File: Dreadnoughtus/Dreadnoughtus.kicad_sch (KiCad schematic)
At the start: 403 parts

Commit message: finalized matrix connections
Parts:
- removed D? (x13): DIODE, symbol Simulation_SPICE:DIODE
- removed MX? (x13): MX-NoLED, symbol MX_Alps_Hybrid:MX-NoLED
- added U?: Elite-C, symbol keebio:Elite-C
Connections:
- net row0: now also U?.5 (2/PD1)
- net row1: now also U?.6 (3/PD0)
- net row10: now also U?.18 (A1/PF6)
- net row11: now also U?.17 (A0/PF7)
- net row12: now also U?.16 (15/PB1)
- net row13: now also U?.15 (14/PB3)
- net row2: now also U?.7 (4/PD4)
- net row3: now also U?.8 (5/PC6)
- net row4: now also U?.9 (6/PD7)
- net row5: now also U?.10 (7/PE6)
- net row6: now also U?.11 (8/PB4)
- net row7: now also U?.12 (9/PB5)
- net row8: now also U?.20 (A3/PF4)
- net row9: now also U?.19 (A2/PF5)
- net at D?.2 (K), D?.2 (K), D?.2 (K)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: now also D?.1 (A) (x10)
- net at D?.2 (K), D?.2 (K): now also D?.1 (A)
- net at D?.2 (K), D?.2 (K), D?.2 (K)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: now also D?.1 (A), D?.2 (K), D?.2 (K), D?.2 (K), D?.2 (K), D?.2 (K), D?.2 (K), D?.2 (K)
- new net row14: U?.14 (16/PB2)
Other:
- moved on the sheet: D?, MX?

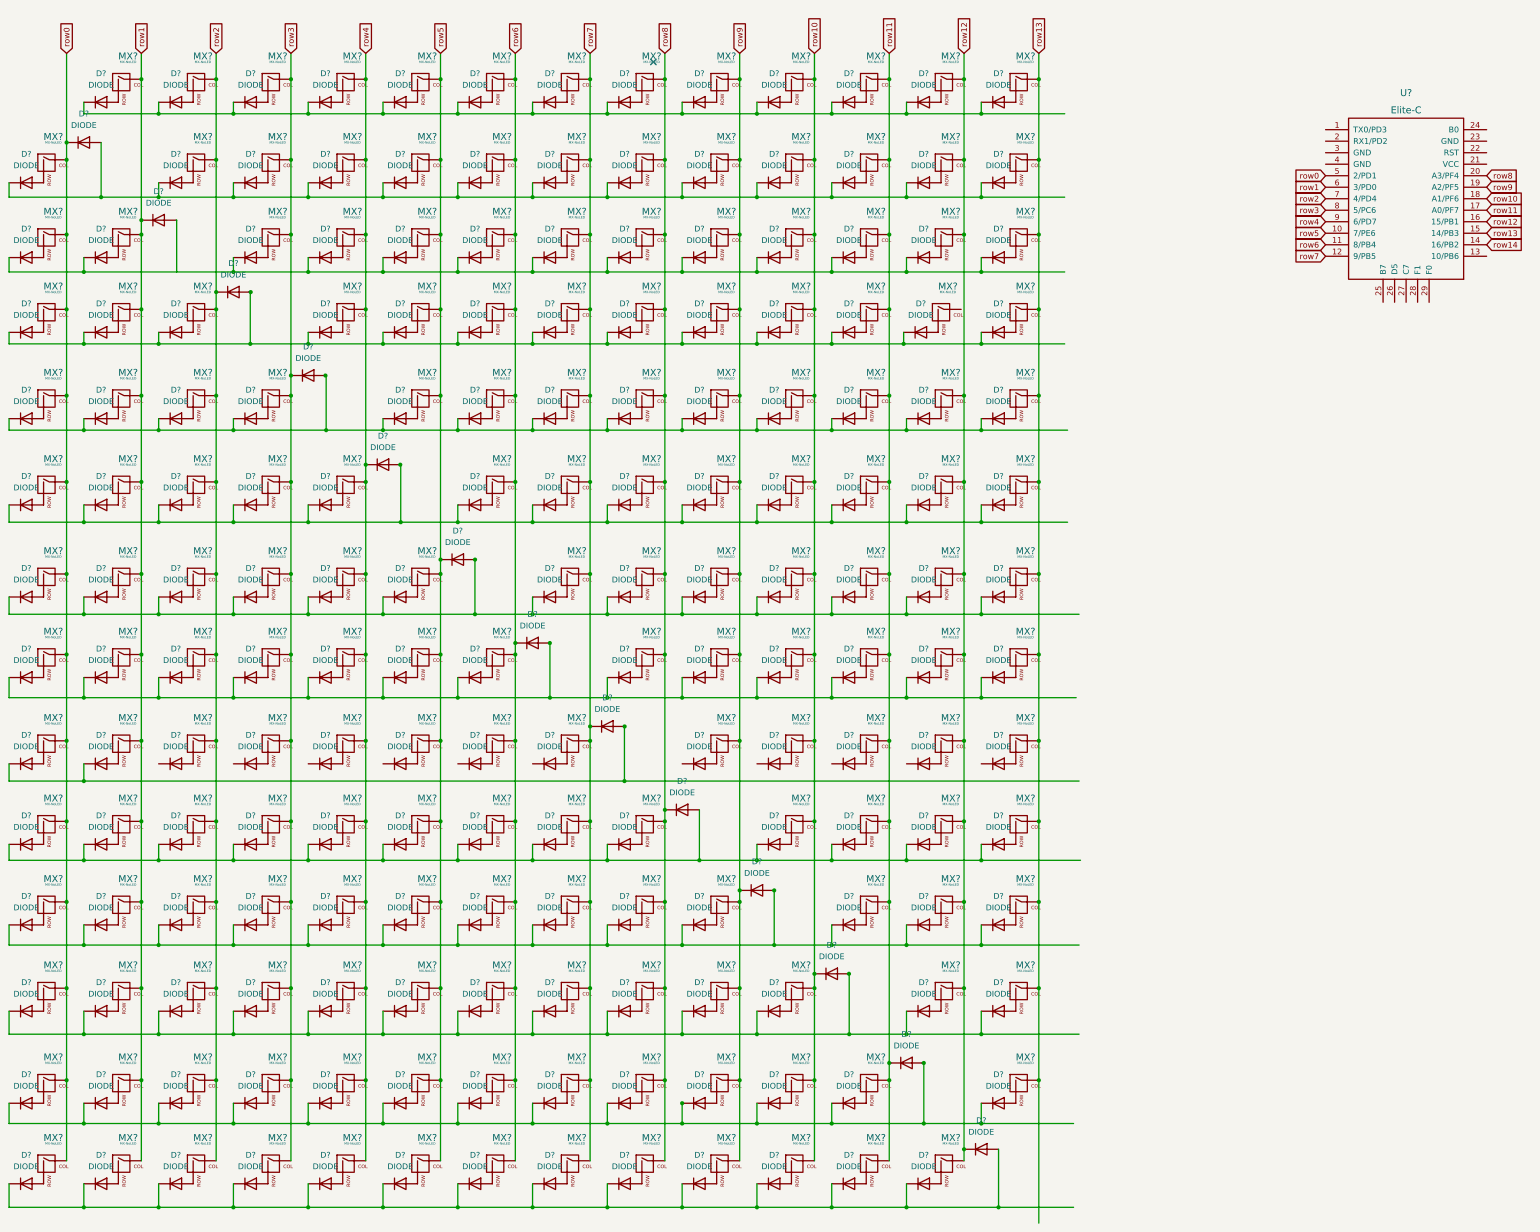
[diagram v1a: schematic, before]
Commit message: named switches and switch diodes, added i2c start schematic
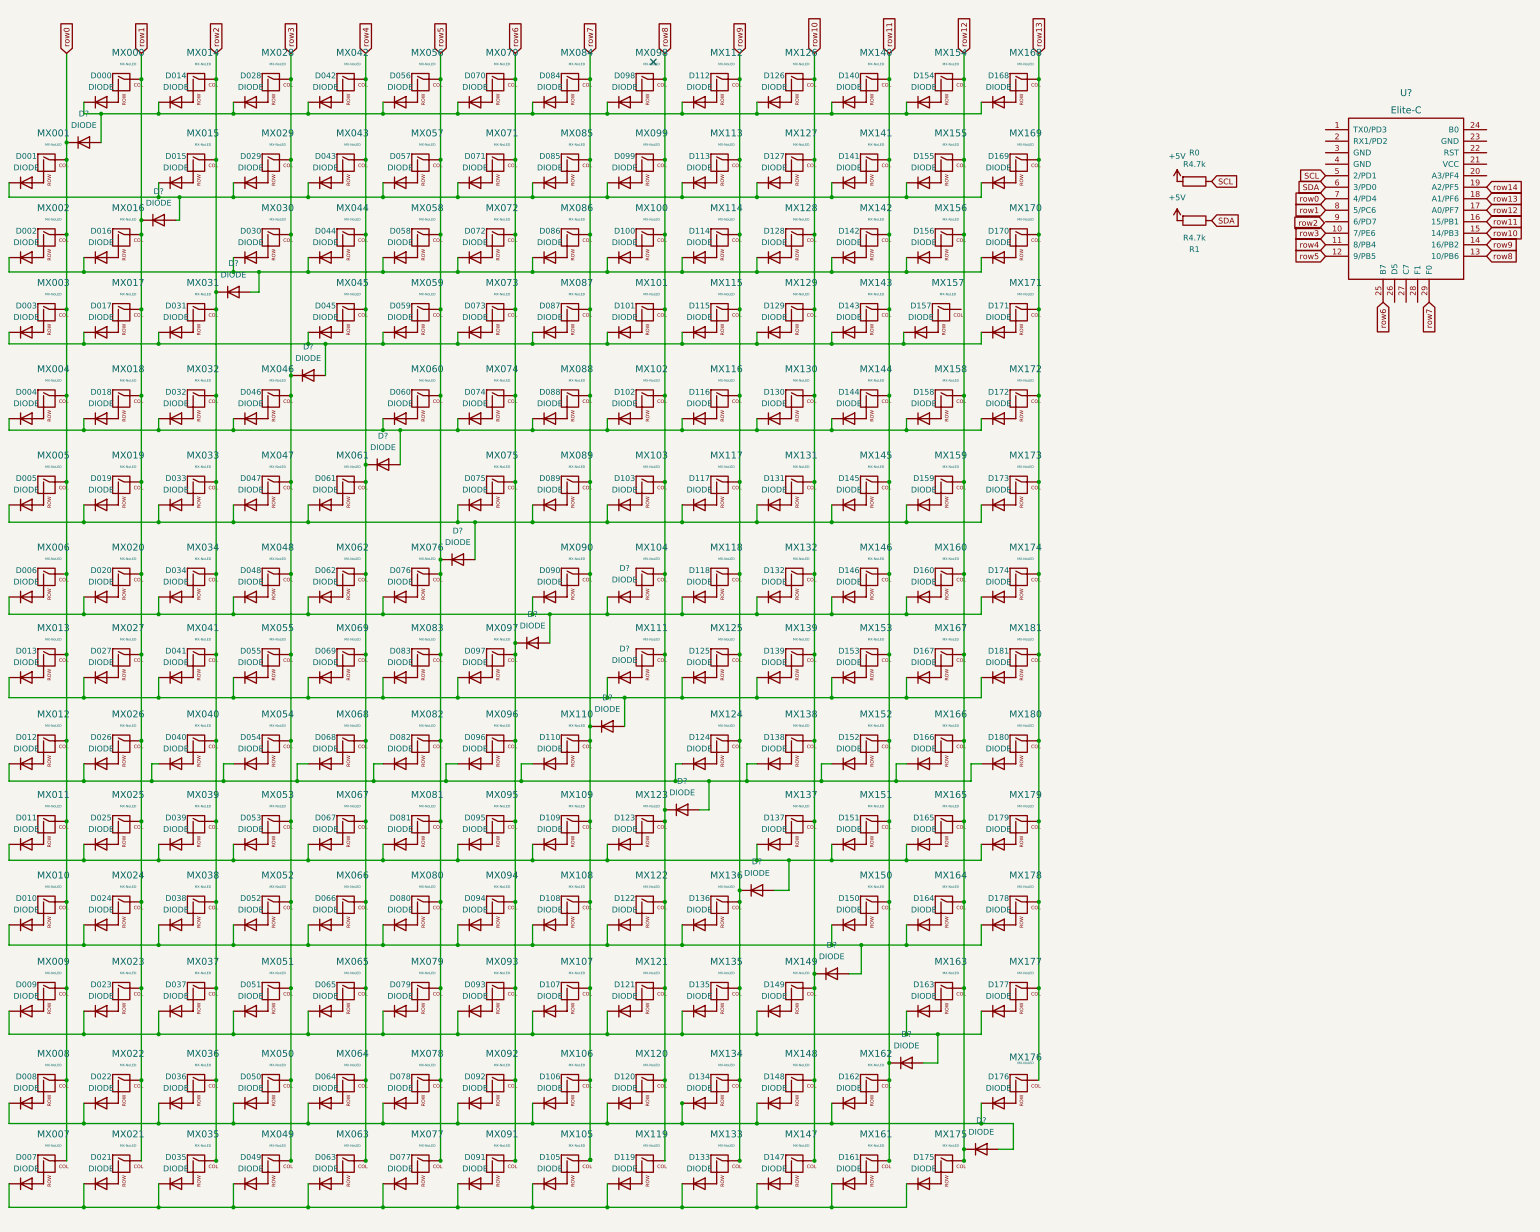
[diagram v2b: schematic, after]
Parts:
- added R0, R1: R4.7k, symbol Device:R
- gave numbers to parts that had none: 362
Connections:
- net row0: now also U?.7 (4/PD4); no longer U?.5 (2/PD1)
- net row1: now also U?.8 (5/PC6); no longer U?.6 (3/PD0)
- net row10: now also U?.15 (14/PB3); no longer U?.18 (A1/PF6)
- net row11: now also U?.16 (15/PB1); no longer U?.17 (A0/PF7)
- net row12: now also U?.17 (A0/PF7); no longer U?.16 (15/PB1)
- net row13: now also U?.18 (A1/PF6); no longer U?.15 (14/PB3)
- net row14: now also U?.19 (A2/PF5); no longer U?.14 (16/PB2)
- net row2: no longer U?.7 (4/PD4)
- net row3: now also U?.10 (7/PE6); no longer U?.8 (5/PC6)
- net row4: now also U?.11 (8/PB4); no longer U?.9 (6/PD7)
- net row5: now also U?.12 (9/PB5); no longer U?.10 (7/PE6)
- net row6: now also U?.25 (B7); no longer U?.11 (8/PB4)
- net row7: now also U?.29 (F0); no longer U?.12 (9/PB5)
- net row8: now also U?.13 (10/PB6); no longer U?.20 (A3/PF4)
- net row9: now also U?.14 (16/PB2); no longer U?.19 (A2/PF5)
- net at D005.2 (K), D019.2 (K), D033.2 (K)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: now also D?.1 (A); no longer D?.1 (A)
- net at D004.2 (K), D018.2 (K), D032.2 (K)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: now also D?.1 (A); no longer D?.1 (A)
- net at D000.2 (K), D014.2 (K), D028.2 (K)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: now also D?.1 (A)
- net at D011.2 (K), D025.2 (K), D039.2 (K)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: now also D?.1 (A); no longer D?.1 (A)
- net at D002.2 (K), D016.2 (K), D030.2 (K)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: now also D?.1 (A)
- net at D003.2 (K), D017.2 (K), D031.2 (K)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: now also D?.1 (A); no longer D?.1 (A)
- net at D010.2 (K), D024.2 (K), D038.2 (K)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: now also D?.1 (A); no longer D?.1 (A)
- net at D007.2 (K), D021.2 (K), D035.2 (K)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: no longer D?.1 (A)
- net at D006.2 (K), D020.2 (K), D034.2 (K)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: now also D?.1 (A); no longer D?.1 (A)
- net at D008.2 (K), D022.2 (K), D036.2 (K)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: now also D?.1 (A); no longer D?.1 (A)
- net at D009.2 (K), D023.2 (K), D037.2 (K)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: now also D?.1 (A); no longer D?.1 (A)
- net at D001.2 (K), D015.2 (K), D029.2 (K)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: now also D?.1 (A); no longer D?.1 (A)
- net at D040.2 (K): now also D012.2 (K), D026.2 (K), D054.2 (K), D068.2 (K), D082.2 (K), D096.2 (K), D110.2 (K), D124.2 (K), D138.2 (K), D152.2 (K), D166.2 (K), D180.2 (K), D?.1 (A)
- net at D013.2 (K), D027.2 (K), D041.2 (K)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: now also D?.1 (A); no longer D?.1 (A)
- new net +5V: R0.2, R1.2
- new net SCL: R0.1, U?.5 (2/PD1)
- new net SDA: R1.1, U?.6 (3/PD0)

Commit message: arranged switches on pcb
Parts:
- added U2, U3: PRTR5V0U2X, Keebio-Parts:I2C_Breakout, symbol keebio:PRTR5V0U2X
- D0: renamed from D000; footprint (none) -> Keebio-Parts:Diode-dual
- D1: renamed from D001; footprint (none) -> Keebio-Parts:Diode-dual
- D10: renamed from D010; footprint (none) -> Keebio-Parts:Diode-dual
- D100, D101, D102, D103, D105, D106, D107, D108, D109, D110, D112, D113, D114, D115, D116, D117, D118, D119, D120, D121, D122, D123, D124, D125, D126, D127, D128, D129, D130, D131, D132, D133, D134, D135, D136, D137, D138, D139, D140, D141, D142, D143, D144, D145, D146, D147, D148, D149, D150, D151, D152, D153, D154, D155, D156, D157, D158, D159, D160, D161, D162, D163, D164, D165, D166, D167, D168, D169, D170, D171, D172, D173, D174, D175, D176, D177, D178, D179, D180, D181: footprint (none) -> Keebio-Parts:Diode-dual
- D104, D111, D201, D202, D203, D204, D205, D206, D207, D208, D209, D210, D211, D212, D213: renamed from D?; footprint (none) -> Keebio-Parts:Diode-dual
- D11: renamed from D011; footprint (none) -> Keebio-Parts:Diode-dual
- D12: renamed from D012; footprint (none) -> Keebio-Parts:Diode-dual
- D13: renamed from D013; footprint (none) -> Keebio-Parts:Diode-dual
- D14: renamed from D014; footprint (none) -> Keebio-Parts:Diode-dual
- D15: renamed from D015; footprint (none) -> Keebio-Parts:Diode-dual
- D16: renamed from D016; footprint (none) -> Keebio-Parts:Diode-dual
- D17: renamed from D017; footprint (none) -> Keebio-Parts:Diode-dual
- D18: renamed from D018; footprint (none) -> Keebio-Parts:Diode-dual
- D19: renamed from D019; footprint (none) -> Keebio-Parts:Diode-dual
- D2: renamed from D002; footprint (none) -> Keebio-Parts:Diode-dual
- D20: renamed from D020; footprint (none) -> Keebio-Parts:Diode-dual
- D21: renamed from D021; footprint (none) -> Keebio-Parts:Diode-dual
- D22: renamed from D022; footprint (none) -> Keebio-Parts:Diode-dual
- D23: renamed from D023; footprint (none) -> Keebio-Parts:Diode-dual
- D24: renamed from D024; footprint (none) -> Keebio-Parts:Diode-dual
- D25: renamed from D025; footprint (none) -> Keebio-Parts:Diode-dual
- D26: renamed from D026; footprint (none) -> Keebio-Parts:Diode-dual
- D27: renamed from D027; footprint (none) -> Keebio-Parts:Diode-dual
- D28: renamed from D028; footprint (none) -> Keebio-Parts:Diode-dual
- D29: renamed from D029; footprint (none) -> Keebio-Parts:Diode-dual
- D3: renamed from D003; footprint (none) -> Keebio-Parts:Diode-dual
- D30: renamed from D030; footprint (none) -> Keebio-Parts:Diode-dual
- D31: renamed from D031; footprint (none) -> Keebio-Parts:Diode-dual
- D32: renamed from D032; footprint (none) -> Keebio-Parts:Diode-dual
- D33: renamed from D033; footprint (none) -> Keebio-Parts:Diode-dual
- D34: renamed from D034; footprint (none) -> Keebio-Parts:Diode-dual
- D35: renamed from D035; footprint (none) -> Keebio-Parts:Diode-dual
- D36: renamed from D036; footprint (none) -> Keebio-Parts:Diode-dual
- D37: renamed from D037; footprint (none) -> Keebio-Parts:Diode-dual
- D38: renamed from D038; footprint (none) -> Keebio-Parts:Diode-dual
- D39: renamed from D039; footprint (none) -> Keebio-Parts:Diode-dual
- D4: renamed from D004; footprint (none) -> Keebio-Parts:Diode-dual
- D40: renamed from D040; footprint (none) -> Keebio-Parts:Diode-dual
- D41: renamed from D041; footprint (none) -> Keebio-Parts:Diode-dual
- D42: renamed from D042; footprint (none) -> Keebio-Parts:Diode-dual
- D43: renamed from D043; footprint (none) -> Keebio-Parts:Diode-dual
- D44: renamed from D044; footprint (none) -> Keebio-Parts:Diode-dual
- D45: renamed from D045; footprint (none) -> Keebio-Parts:Diode-dual
- D46: renamed from D046; footprint (none) -> Keebio-Parts:Diode-dual
- D47: renamed from D047; footprint (none) -> Keebio-Parts:Diode-dual
- D48: renamed from D048; footprint (none) -> Keebio-Parts:Diode-dual
- D49: renamed from D049; footprint (none) -> Keebio-Parts:Diode-dual
- D5: renamed from D005; footprint (none) -> Keebio-Parts:Diode-dual
- D50: renamed from D050; footprint (none) -> Keebio-Parts:Diode-dual
- D51: renamed from D051; footprint (none) -> Keebio-Parts:Diode-dual
- D52: renamed from D052; footprint (none) -> Keebio-Parts:Diode-dual
- D53: renamed from D053; footprint (none) -> Keebio-Parts:Diode-dual
- D54: renamed from D054; footprint (none) -> Keebio-Parts:Diode-dual
- D55: renamed from D055; footprint (none) -> Keebio-Parts:Diode-dual
- D56: renamed from D056; footprint (none) -> Keebio-Parts:Diode-dual
- D57: renamed from D057; footprint (none) -> Keebio-Parts:Diode-dual
- D58: renamed from D058; footprint (none) -> Keebio-Parts:Diode-dual
- D59: renamed from D059; footprint (none) -> Keebio-Parts:Diode-dual
- D6: renamed from D006; footprint (none) -> Keebio-Parts:Diode-dual
- D60: renamed from D060; footprint (none) -> Keebio-Parts:Diode-dual
- D61: renamed from D061; footprint (none) -> Keebio-Parts:Diode-dual
- D62: renamed from D062; footprint (none) -> Keebio-Parts:Diode-dual
- D63: renamed from D063; footprint (none) -> Keebio-Parts:Diode-dual
- D64: renamed from D064; footprint (none) -> Keebio-Parts:Diode-dual
- D65: renamed from D065; footprint (none) -> Keebio-Parts:Diode-dual
- D66: renamed from D066; footprint (none) -> Keebio-Parts:Diode-dual
- D67: renamed from D067; footprint (none) -> Keebio-Parts:Diode-dual
- D68: renamed from D068; footprint (none) -> Keebio-Parts:Diode-dual
- D69: renamed from D069; footprint (none) -> Keebio-Parts:Diode-dual
- D7: renamed from D007; footprint (none) -> Keebio-Parts:Diode-dual
- D70: renamed from D070; footprint (none) -> Keebio-Parts:Diode-dual
- D71: renamed from D071; footprint (none) -> Keebio-Parts:Diode-dual
- D72: renamed from D072; footprint (none) -> Keebio-Parts:Diode-dual
- D73: renamed from D073; footprint (none) -> Keebio-Parts:Diode-dual
- D74: renamed from D074; footprint (none) -> Keebio-Parts:Diode-dual
- D75: renamed from D075; footprint (none) -> Keebio-Parts:Diode-dual
- D76: renamed from D076; footprint (none) -> Keebio-Parts:Diode-dual
- D77: renamed from D077; footprint (none) -> Keebio-Parts:Diode-dual
- D78: renamed from D078; footprint (none) -> Keebio-Parts:Diode-dual
- D79: renamed from D079; footprint (none) -> Keebio-Parts:Diode-dual
- D8: renamed from D008; footprint (none) -> Keebio-Parts:Diode-dual
- D80: renamed from D080; footprint (none) -> Keebio-Parts:Diode-dual
- D81: renamed from D081; footprint (none) -> Keebio-Parts:Diode-dual
- D82: renamed from D082; footprint (none) -> Keebio-Parts:Diode-dual
- D83: renamed from D083; footprint (none) -> Keebio-Parts:Diode-dual
- D84: renamed from D084; footprint (none) -> Keebio-Parts:Diode-dual
- D85: renamed from D085; footprint (none) -> Keebio-Parts:Diode-dual
- D86: renamed from D086; footprint (none) -> Keebio-Parts:Diode-dual
- D87: renamed from D087; footprint (none) -> Keebio-Parts:Diode-dual
- D88: renamed from D088; footprint (none) -> Keebio-Parts:Diode-dual
- D89: renamed from D089; footprint (none) -> Keebio-Parts:Diode-dual
- D9: renamed from D009; footprint (none) -> Keebio-Parts:Diode-dual
- D90: renamed from D090; footprint (none) -> Keebio-Parts:Diode-dual
- D91: renamed from D091; footprint (none) -> Keebio-Parts:Diode-dual
- D92: renamed from D092; footprint (none) -> Keebio-Parts:Diode-dual
- D93: renamed from D093; footprint (none) -> Keebio-Parts:Diode-dual
- D94: renamed from D094; footprint (none) -> Keebio-Parts:Diode-dual
- D95: renamed from D095; footprint (none) -> Keebio-Parts:Diode-dual
- D96: renamed from D096; footprint (none) -> Keebio-Parts:Diode-dual
- D97: renamed from D097; footprint (none) -> Keebio-Parts:Diode-dual
- D98: renamed from D098; footprint (none) -> Keebio-Parts:Diode-dual
- D99: renamed from D099; footprint (none) -> Keebio-Parts:Diode-dual
- MX0: renamed from MX000; footprint (none) -> MX_Alps_Hybrid:MXOnly-1U-Hotswap
- MX1: renamed from MX001; footprint (none) -> MX_Alps_Hybrid:MXOnly-1U-Hotswap
- MX10: renamed from MX010; footprint (none) -> MX_Alps_Hybrid:MXOnly-1U-Hotswap
- MX100, MX101, MX102, MX103, MX104, MX105, MX106, MX107, MX108, MX109, MX110, MX111, MX112, MX113, MX114, MX115, MX116, MX117, MX118, MX119, MX120, MX121, MX122, MX123, MX124, MX125, MX126, MX127, MX128, MX129, MX130, MX131, MX132, MX133, MX134, MX135, MX136, MX137, MX138, MX139, MX140, MX141, MX142, MX143, MX144, MX145, MX146, MX147, MX148, MX149, MX150, MX151, MX152, MX153, MX154, MX155, MX156, MX157, MX158, MX159, MX160, MX161, MX162, MX163, MX164, MX165, MX166, MX167, MX168, MX169, MX170, MX171, MX172, MX173, MX174, MX175, MX176, MX177, MX178, MX179, MX180, MX181: footprint (none) -> MX_Alps_Hybrid:MXOnly-1U-Hotswap
- MX11: renamed from MX011; footprint (none) -> MX_Alps_Hybrid:MXOnly-1U-Hotswap
- MX12: renamed from MX012; footprint (none) -> MX_Alps_Hybrid:MXOnly-1U-Hotswap
- MX13: renamed from MX013; footprint (none) -> MX_Alps_Hybrid:MXOnly-1U-Hotswap
- MX14: renamed from MX014; footprint (none) -> MX_Alps_Hybrid:MXOnly-1U-Hotswap
- MX15: renamed from MX015; footprint (none) -> MX_Alps_Hybrid:MXOnly-1U-Hotswap
- MX16: renamed from MX016; footprint (none) -> MX_Alps_Hybrid:MXOnly-1U-Hotswap
- MX17: renamed from MX017; footprint (none) -> MX_Alps_Hybrid:MXOnly-1U-Hotswap
- MX18: renamed from MX018; footprint (none) -> MX_Alps_Hybrid:MXOnly-1U-Hotswap
- MX19: renamed from MX019; footprint (none) -> MX_Alps_Hybrid:MXOnly-1U-Hotswap
- MX2: renamed from MX002; footprint (none) -> MX_Alps_Hybrid:MXOnly-1U-Hotswap
- MX20: renamed from MX020; footprint (none) -> MX_Alps_Hybrid:MXOnly-1U-Hotswap
- MX21: renamed from MX021; footprint (none) -> MX_Alps_Hybrid:MXOnly-1U-Hotswap
- MX22: renamed from MX022; footprint (none) -> MX_Alps_Hybrid:MXOnly-1U-Hotswap
- MX23: renamed from MX023; footprint (none) -> MX_Alps_Hybrid:MXOnly-1U-Hotswap
- MX24: renamed from MX024; footprint (none) -> MX_Alps_Hybrid:MXOnly-1U-Hotswap
- MX25: renamed from MX025; footprint (none) -> MX_Alps_Hybrid:MXOnly-1U-Hotswap
- MX26: renamed from MX026; footprint (none) -> MX_Alps_Hybrid:MXOnly-1U-Hotswap
- MX27: renamed from MX027; footprint (none) -> MX_Alps_Hybrid:MXOnly-1U-Hotswap
- MX28: renamed from MX028; footprint (none) -> MX_Alps_Hybrid:MXOnly-1U-Hotswap
- MX29: renamed from MX029; footprint (none) -> MX_Alps_Hybrid:MXOnly-1U-Hotswap
- MX3: renamed from MX003; footprint (none) -> MX_Alps_Hybrid:MXOnly-1U-Hotswap
- MX30: renamed from MX030; footprint (none) -> MX_Alps_Hybrid:MXOnly-1U-Hotswap
- MX31: renamed from MX031; footprint (none) -> MX_Alps_Hybrid:MXOnly-1U-Hotswap
- MX32: renamed from MX032; footprint (none) -> MX_Alps_Hybrid:MXOnly-1U-Hotswap
- MX33: renamed from MX033; footprint (none) -> MX_Alps_Hybrid:MXOnly-1U-Hotswap
- MX34: renamed from MX034; footprint (none) -> MX_Alps_Hybrid:MXOnly-1U-Hotswap
- MX35: renamed from MX035; footprint (none) -> MX_Alps_Hybrid:MXOnly-1U-Hotswap
- MX36: renamed from MX036; footprint (none) -> MX_Alps_Hybrid:MXOnly-1U-Hotswap
- MX37: renamed from MX037; footprint (none) -> MX_Alps_Hybrid:MXOnly-1U-Hotswap
- MX38: renamed from MX038; footprint (none) -> MX_Alps_Hybrid:MXOnly-1U-Hotswap
- MX39: renamed from MX039; footprint (none) -> MX_Alps_Hybrid:MXOnly-1U-Hotswap
- MX4: renamed from MX004; footprint (none) -> MX_Alps_Hybrid:MXOnly-1U-Hotswap
- MX40: renamed from MX040; footprint (none) -> MX_Alps_Hybrid:MXOnly-1U-Hotswap
- MX41: renamed from MX041; footprint (none) -> MX_Alps_Hybrid:MXOnly-1U-Hotswap
- MX42: renamed from MX042; footprint (none) -> MX_Alps_Hybrid:MXOnly-1U-Hotswap
- MX43: renamed from MX043; footprint (none) -> MX_Alps_Hybrid:MXOnly-1U-Hotswap
- MX44: renamed from MX044; footprint (none) -> MX_Alps_Hybrid:MXOnly-1U-Hotswap
- MX45: renamed from MX045; footprint (none) -> MX_Alps_Hybrid:MXOnly-1U-Hotswap
- MX46: renamed from MX046; footprint (none) -> MX_Alps_Hybrid:MXOnly-1U-Hotswap
- MX47: renamed from MX047; footprint (none) -> MX_Alps_Hybrid:MXOnly-1U-Hotswap
- MX48: renamed from MX048; footprint (none) -> MX_Alps_Hybrid:MXOnly-1U-Hotswap
- MX49: renamed from MX049; footprint (none) -> MX_Alps_Hybrid:MXOnly-1U-Hotswap
- MX5: renamed from MX005; footprint (none) -> MX_Alps_Hybrid:MXOnly-1U-Hotswap
- MX50: renamed from MX050; footprint (none) -> MX_Alps_Hybrid:MXOnly-1U-Hotswap
- MX51: renamed from MX051; footprint (none) -> MX_Alps_Hybrid:MXOnly-1U-Hotswap
- MX52: renamed from MX052; footprint (none) -> MX_Alps_Hybrid:MXOnly-1U-Hotswap
- MX53: renamed from MX053; footprint (none) -> MX_Alps_Hybrid:MXOnly-1U-Hotswap
- MX54: renamed from MX054; footprint (none) -> MX_Alps_Hybrid:MXOnly-1U-Hotswap
- MX55: renamed from MX055; footprint (none) -> MX_Alps_Hybrid:MXOnly-1U-Hotswap
- MX56: renamed from MX056; footprint (none) -> MX_Alps_Hybrid:MXOnly-1U-Hotswap
- MX57: renamed from MX057; footprint (none) -> MX_Alps_Hybrid:MXOnly-1U-Hotswap
- MX58: renamed from MX058; footprint (none) -> MX_Alps_Hybrid:MXOnly-1U-Hotswap
- MX59: renamed from MX059; footprint (none) -> MX_Alps_Hybrid:MXOnly-1U-Hotswap
- MX6: renamed from MX006; footprint (none) -> MX_Alps_Hybrid:MXOnly-1U-Hotswap
- MX60: renamed from MX060; footprint (none) -> MX_Alps_Hybrid:MXOnly-1U-Hotswap
- MX61: renamed from MX061; footprint (none) -> MX_Alps_Hybrid:MXOnly-1U-Hotswap
- MX62: renamed from MX062; footprint (none) -> MX_Alps_Hybrid:MXOnly-1U-Hotswap
- MX63: renamed from MX063; footprint (none) -> MX_Alps_Hybrid:MXOnly-1U-Hotswap
- MX64: renamed from MX064; footprint (none) -> MX_Alps_Hybrid:MXOnly-1U-Hotswap
- MX65: renamed from MX065; footprint (none) -> MX_Alps_Hybrid:MXOnly-1U-Hotswap
- MX66: renamed from MX066; footprint (none) -> MX_Alps_Hybrid:MXOnly-1U-Hotswap
- MX67: renamed from MX067; footprint (none) -> MX_Alps_Hybrid:MXOnly-1U-Hotswap
- MX68: renamed from MX068; footprint (none) -> MX_Alps_Hybrid:MXOnly-1U-Hotswap
- MX69: renamed from MX069; footprint (none) -> MX_Alps_Hybrid:MXOnly-1U-Hotswap
- MX7: renamed from MX007; footprint (none) -> MX_Alps_Hybrid:MXOnly-1U-Hotswap
- MX70: renamed from MX070; footprint (none) -> MX_Alps_Hybrid:MXOnly-1U-Hotswap
- MX71: renamed from MX071; footprint (none) -> MX_Alps_Hybrid:MXOnly-1U-Hotswap
- MX72: renamed from MX072; footprint (none) -> MX_Alps_Hybrid:MXOnly-1U-Hotswap
- MX73: renamed from MX073; footprint (none) -> MX_Alps_Hybrid:MXOnly-1U-Hotswap
- MX74: renamed from MX074; footprint (none) -> MX_Alps_Hybrid:MXOnly-1U-Hotswap
- MX75: renamed from MX075; footprint (none) -> MX_Alps_Hybrid:MXOnly-1U-Hotswap
- MX76: renamed from MX076; footprint (none) -> MX_Alps_Hybrid:MXOnly-1U-Hotswap
- MX77: renamed from MX077; footprint (none) -> MX_Alps_Hybrid:MXOnly-1U-Hotswap
- MX78: renamed from MX078; footprint (none) -> MX_Alps_Hybrid:MXOnly-1U-Hotswap
- MX79: renamed from MX079; footprint (none) -> MX_Alps_Hybrid:MXOnly-1U-Hotswap
- MX8: renamed from MX008; footprint (none) -> MX_Alps_Hybrid:MXOnly-1U-Hotswap
- MX80: renamed from MX080; footprint (none) -> MX_Alps_Hybrid:MXOnly-1U-Hotswap
- MX81: renamed from MX081; footprint (none) -> MX_Alps_Hybrid:MXOnly-1U-Hotswap
- MX82: renamed from MX082; footprint (none) -> MX_Alps_Hybrid:MXOnly-1U-Hotswap
- MX83: renamed from MX083; footprint (none) -> MX_Alps_Hybrid:MXOnly-1U-Hotswap
- MX84: renamed from MX084; footprint (none) -> MX_Alps_Hybrid:MXOnly-1U-Hotswap
- MX85: renamed from MX085; footprint (none) -> MX_Alps_Hybrid:MXOnly-1U-Hotswap
- MX86: renamed from MX086; footprint (none) -> MX_Alps_Hybrid:MXOnly-1U-Hotswap
- MX87: renamed from MX087; footprint (none) -> MX_Alps_Hybrid:MXOnly-1U-Hotswap
- MX88: renamed from MX088; footprint (none) -> MX_Alps_Hybrid:MXOnly-1U-Hotswap
- MX89: renamed from MX089; footprint (none) -> MX_Alps_Hybrid:MXOnly-1U-Hotswap
- MX9: renamed from MX009; footprint (none) -> MX_Alps_Hybrid:MXOnly-1U-Hotswap
- MX90: renamed from MX090; footprint (none) -> MX_Alps_Hybrid:MXOnly-1U-Hotswap
- MX91: renamed from MX091; footprint (none) -> MX_Alps_Hybrid:MXOnly-1U-Hotswap
- MX92: renamed from MX092; footprint (none) -> MX_Alps_Hybrid:MXOnly-1U-Hotswap
- MX93: renamed from MX093; footprint (none) -> MX_Alps_Hybrid:MXOnly-1U-Hotswap
- MX94: renamed from MX094; footprint (none) -> MX_Alps_Hybrid:MXOnly-1U-Hotswap
- MX95: renamed from MX095; footprint (none) -> MX_Alps_Hybrid:MXOnly-1U-Hotswap
- MX96: renamed from MX096; footprint (none) -> MX_Alps_Hybrid:MXOnly-1U-Hotswap
- MX97: renamed from MX097; footprint (none) -> MX_Alps_Hybrid:MXOnly-1U-Hotswap
- MX98: renamed from MX098; footprint (none) -> MX_Alps_Hybrid:MXOnly-1U-Hotswap
- MX99: renamed from MX099; footprint (none) -> MX_Alps_Hybrid:MXOnly-1U-Hotswap
- R0, R1: footprint (none) -> Keebio-Parts:Resistor
- U1: renamed from U?; footprint (none) -> Keebio-Parts:Elite-C-castellated-29pin-holes
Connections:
- net +5V: now also U1.21 (VCC), U2.4 (VCC)
- net SCL: now also U2.3 (I/O2)
- net SDA: now also U2.2 (I/O1)
- net row12: now also MX157.1 (COL)
- net row2: now also U1.9 (6/PD7)
- net reset: now reaches U1.22 (RST)
- net reset: now also U3.2 (I/O1)
- net GND1: now reaches U1.23 (GND)
- net GND1: now also U1.3 (GND), U1.4 (GND), U2.1 (GND), U3.1 (GND)
- net row14: no longer names the net of U1.19 (A2/PF5)
- no-connect marks 1 -> 0
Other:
- moved on the sheet: R0, R1
